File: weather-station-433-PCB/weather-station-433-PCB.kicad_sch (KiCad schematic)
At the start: 6 parts, among them Q1 PN2222A, U1 BluePill, U2 DHT11

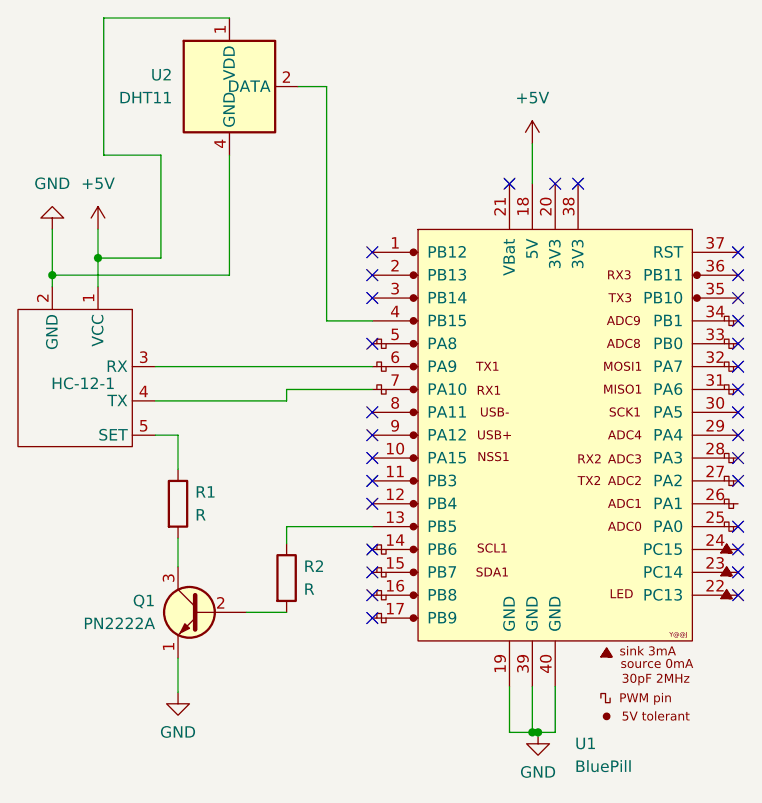
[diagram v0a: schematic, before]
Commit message: Resistance for Q1 calculated Skeleton program for the Firmware created
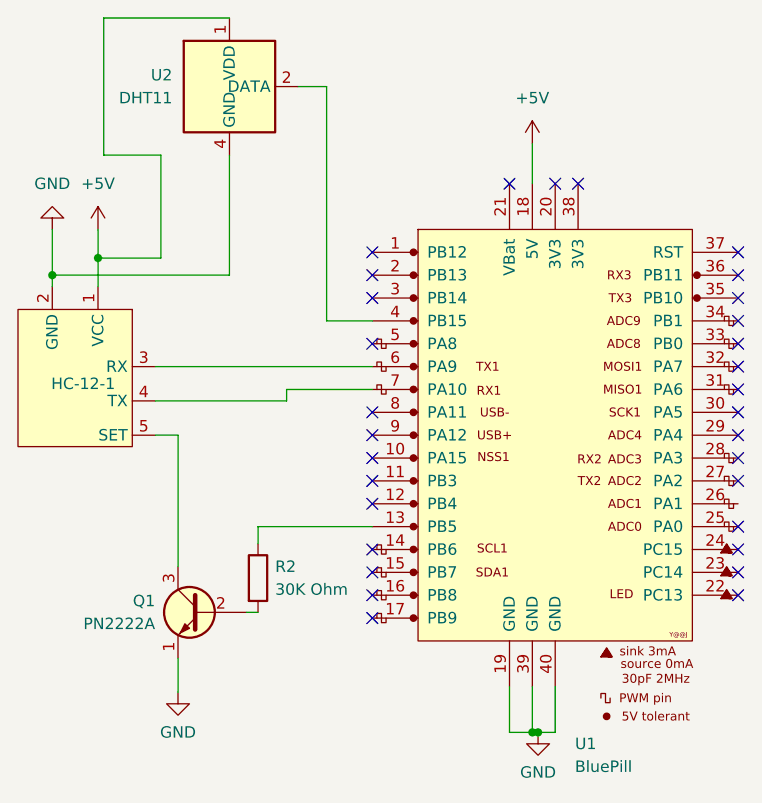
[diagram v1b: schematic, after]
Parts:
- removed R1: R, symbol Device:R
- R2: value R -> 30K Ohm
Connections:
- net at HC-12-1.5 (SET): now also Q1.3 (C)
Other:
- moved on the sheet: R2
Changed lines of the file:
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@@
     (stroke (width 0) (type default))
   )
-  (wire (pts (xy 107.315 109.855) (xy 111.76 109.855))
+  (wire (pts (xy 107.315 109.855) (xy 108.585 109.855))
+    (stroke (width 0) (type default))
+  )
+  (wire (pts (xy 108.585 100.33) (xy 108.585 102.235))
     (stroke (width 0) (type default))
   )
@@
     (stroke (width 0) (type default))
   )
-  (wire (pts (xy 111.76 100.33) (xy 121.285 100.33))
+  (wire (pts (xy 108.585 100.33) (xy 121.285 100.33))
     (stroke (width 0) (type default))
   )
@@
     (stroke (width 0) (type default))
   )
-  (wire (pts (xy 99.695 101.6) (xy 99.695 104.775))
-    (stroke (width 0) (type default))
-  )
-  (wire (pts (xy 111.76 102.235) (xy 111.76 100.33))
-    (stroke (width 0) (type default))
-  )
   (wire (pts (xy 97.155 86.36) (xy 111.76 86.36))
     (stroke (width 0) (type default))
@@
     (stroke (width 0) (type default))
   )
-  (wire (pts (xy 99.695 90.17) (xy 99.695 93.98))
+  (wire (pts (xy 99.695 90.17) (xy 99.695 104.775))
     (stroke (width 0) (type default))
   )
@@
     )
   )
-  (symbol (lib_id "Device:R") (at 111.76 106.045 0) (unit 1)
-    (in_bom yes) (on_board yes) (dnp no) (fields_autoplaced)
-    (property "Reference" "R2" (at 113.665 104.775 0)
-      (effects (font (size 1.27 1.27)) (justify left))
-    )
-    (property "Value" "R" (at 113.665 107.315 0)
-      (effects (font (size 1.27 1.27)) (justify left))
-    )
-    (property "Footprint" "" (at 109.982 106.045 90)
-      (effects (font (size 1.27 1.27)) hide)
-    )
-    (property "Datasheet" "~" (at 111.76 106.045 0)
+  (symbol (lib_id "Device:R") (at 108.585 106.045 0) (unit 1)
+    (in_bom yes) (on_board yes) (dnp no) (fields_autoplaced)
+    (property "Reference" "R2" (at 110.49 104.775 0)
+      (effects (font (size 1.27 1.27)) (justify left))
+    )
+    (property "Value" "30K Ohm" (at 110.49 107.315 0)
+      (effects (font (size 1.27 1.27)) (justify left))
+    )
+    (property "Footprint" "" (at 106.807 106.045 90)
+      (effects (font (size 1.27 1.27)) hide)
+    )
+    (property "Datasheet" "~" (at 108.585 106.045 0)
       (effects (font (size 1.27 1.27)) hide)
     )
@@
         )
       )
-    )
-  )
-  (symbol (lib_id "Device:R") (at 99.695 97.79 0) (unit 1)
-    (in_bom yes) (on_board yes) (dnp no) (fields_autoplaced)
-    (property "Reference" "R1" (at 101.6 96.52 0)
-      (effects (font (size 1.27 1.27)) (justify left))
-    )
-    (property "Value" "R" (at 101.6 99.06 0)
-      (effects (font (size 1.27 1.27)) (justify left))
-    )
-    (property "Footprint" "" (at 97.917 97.79 90)
-      (effects (font (size 1.27 1.27)) hide)
-    )
-    (property "Datasheet" "~" (at 99.695 97.79 0)
-      (effects (font (size 1.27 1.27)) hide)
-    )
-    (pin "2")
-    (pin "1")
-    (instances
-      (project "weather-station-433-PCB"
-        (path "/164d28bf-c209-4f93-a6c5-fe1c21cfd3b5"
-          (reference "R1") (unit 1)
-        )
-      )
